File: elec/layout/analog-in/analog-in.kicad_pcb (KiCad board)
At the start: 2 copper layers, 8 parts, among them U2 1µF ±10% 25V X5R, U3 10kΩ ±1% 62.5mW, U4 10kΩ ±1% 62.5mW, U6 1kΩ ±1% 62.5mW, U7 1kΩ ±1% 62.5mW

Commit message: rebuild all modules
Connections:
- net io renamed top

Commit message: core layout, rebuild modules with compiler updates
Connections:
- U1 pad 10: line-1 -> line
- U1 pad 9: line -> line-1
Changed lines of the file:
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@@
     (net 4 "AIN2")
     (net 5 "AIN1")
-    (net 6 "line")
+    (net 6 "line-1")
     (net 7 "gnd")
-    (net 8 "line-1")
+    (net 8 "line")
     (net 9 "ALERT_slash_RDY")
     (net 10 "amplifier.opamp.footprint.pins[4].net-net")
@@
             (layers "F.Cu" "F.Paste" "F.Mask")
             (remove_unused_layers no)
-            (net 6 "line"))
+            (net 6 "line-1"))
         (pad "10" smd oval
             (at -1 -2.11 90)
@@
             (layers "F.Cu" "F.Paste" "F.Mask")
             (remove_unused_layers no)
-            (net 8 "line-1"))
+            (net 8 "line"))
         (model "/Users/narayanpowderly/projects/hil-blocks/build/footprints/footprints.3dshapes/MSOP-10_L3.0-W3.0-H1.1-LS5.0-P0.50.step"
             (offset

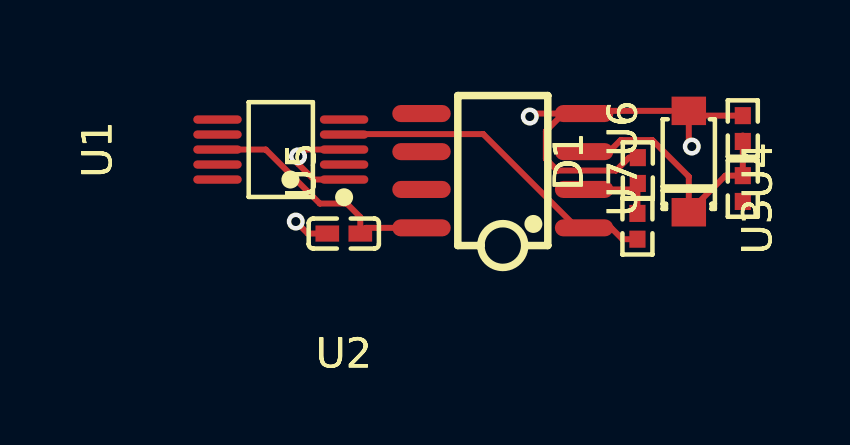
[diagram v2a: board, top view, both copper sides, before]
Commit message: update analog in
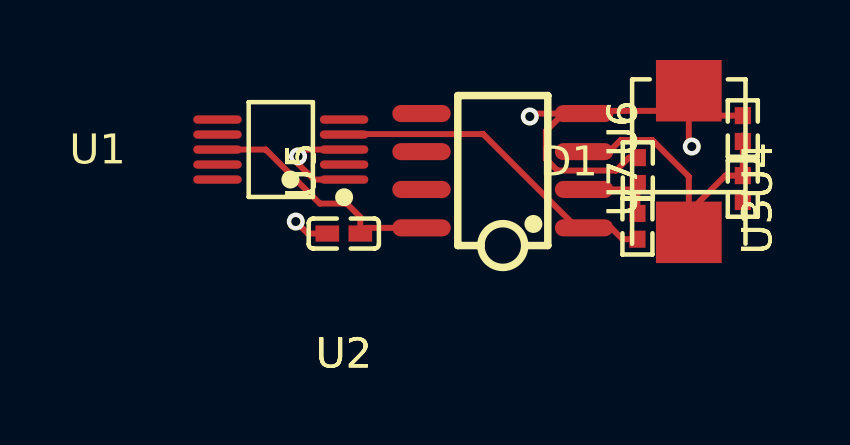
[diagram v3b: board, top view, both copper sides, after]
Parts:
- D1: footprint atopile:SOD-123_L2.8-W1.8-LS3.7-RD-5bef17 -> atopile:SMB_L4.6-W3.6-LS5.3-RD-330cb3
- U1: footprint lib:MSOP-10_L3.0-W3.0-P0.50-LS5.0-BL -> atopile:MSOP-10_L3.0-W3.0-P0.50-LS5.0-BL-752175
- U3, U4: value 10kΩ ±1% 62.5mW -> 1kΩ ±1% 62.5mW
- U5: value (none) -> BW CMRR Ib Vos GBW Iout SR
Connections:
- net AIN1 renamed adc-line-4
- net AIN2 renamed adc-line-2
- net AIN3 renamed adc-line-1
- net ALERT_slash_RDY renamed adc-line-3
- net cathode renamed line-2
- net inverting renamed inverting_input
- U1 pad 10: line -> line-1
- U1 pad 9: line-1 -> line

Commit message: Everything builds
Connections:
- D1 pad 1: line-2 -> line-1
- D1 pad 2: gnd -> adc-line-4
- U1 pad 1: gnd -> adc-line-4
- U1 pad 10: line-1 -> line
- U1 pad 2: adc-line-3 -> adc-line-2
- U1 pad 3: gnd -> adc-line-4
- U1 pad 5: adc-line-4 -> adc-line-3
- U1 pad 6: adc-line-2 -> adc-line-1
- U1 pad 7: adc-line-1 -> adc-line
- U1 pad 9: line -> line-3
- U2 pad 2: gnd -> adc-line-4
- U4 pad 1: gnd -> adc-line-4
- U5 pad 3: line-2 -> line-1
- U5 pad 4: gnd -> adc-line-4
- U6 pad 1: line-2 -> line-1
- U6 pad 2: gnd -> adc-line-4
- U7 pad 1: top -> line-2
- U7 pad 2: line-2 -> line-1
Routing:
- net gnd: track 18.6 -> 0.00 mm, vias 4 -> 0
- net adc-line-4: track 0.00 -> 18.6 mm, vias 0 -> 4
- net line-2: track 8.99 -> 0.00 mm
- net line-1: track 0.00 -> 8.99 mm
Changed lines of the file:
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@@
     (net 0 "")
     (net 1 "amplifier.opamp.footprint.pins[5].net-net")
-    (net 2 "line-2")
+    (net 2 "line-1")
     (net 3 "amplifier.opamp.footprint.pins[6].net-net")
-    (net 4 "adc-line-2")
-    (net 5 "adc-line-4")
-    (net 6 "line")
-    (net 7 "gnd")
-    (net 8 "line-1")
-    (net 9 "adc-line-3")
+    (net 4 "adc-line-1")
+    (net 5 "adc-line-3")
+    (net 6 "line-3")
+    (net 7 "adc-line-4")
+    (net 8 "line")
+    (net 9 "adc-line-2")
     (net 10 "amplifier.opamp.footprint.pins[4].net-net")
-    (net 11 "top")
+    (net 11 "line-2")
     (net 12 "inverting_input")
-    (net 13 "adc-line-1")
+    (net 13 "adc-line")
     (net 14 "output")
     (net 15 "hv")
@@
             (layers "F.Cu" "F.Paste" "F.Mask")
             (remove_unused_layers no)
-            (net 7 "gnd"))
+            (net 7 "adc-line-4"))
         (pad "1" smd rect
             (at -2.36 0 90)
@@
             (layers "F.Cu" "F.Paste" "F.Mask")
             (remove_unused_layers no)
-            (net 2 "line-2")))
+            (net 2 "line-1")))
     (footprint "atopile:SOIC-8_L5.0-W4.0-P1.27-LS6.0-BL-294f77"
         (layer "F.Cu")
@@
             (layers "F.Cu" "F.Paste" "F.Mask")
             (remove_unused_layers no)
-            (net 2 "line-2"))
+            (net 2 "line-1"))
         (pad "4" smd oval
             (at 1.9 2.71 90)
@@
             (layers "F.Cu" "F.Paste" "F.Mask")
             (remove_unused_layers no)
-            (net 7 "gnd"))
+            (net 7 "adc-line-4"))
         (pad "5" smd oval
             (at 1.9 -2.71 90)
@@
             (layers "F.Cu" "F.Paste" "F.Mask")
             (remove_unused_layers no)
-            (net 7 "gnd"))
+            (net 7 "adc-line-4"))
         (pad "2" smd rect
             (at 0.43 0 270)
@@
             (layers "F.Cu" "F.Paste" "F.Mask")
             (remove_unused_layers no)
-            (net 11 "top"))
+            (net 11 "line-2"))
         (pad "2" smd rect
             (at 0.43 0 90)
@@
             (layers "F.Cu" "F.Paste" "F.Mask")
             (remove_unused_layers no)
-            (net 2 "line-2")))
+            (net 2 "line-1")))
     (footprint "atopile:R0402-56259e"
         (layer "F.Cu")
@@
             (layers "F.Cu" "F.Paste" "F.Mask")
             (remove_unused_layers no)
-            (net 2 "line-2"))
+            (net 2 "line-1"))
         (pad "2" smd rect
             (at 0.43 0 90)
@@
             (layers "F.Cu" "F.Paste" "F.Mask")
             (remove_unused_layers no)
-            (net 7 "gnd")))
+            (net 7 "adc-line-4")))
     (footprint "atopile:MSOP-10_L3.0-W3.0-P0.50-LS5.0-BL-752175"
         (layer "F.Cu")
@@
             (layers "F.Cu" "F.Paste" "F.Mask")
             (remove_unused_layers no)
-            (net 7 "gnd"))
+            (net 7 "adc-line-4"))
         (pad "2" smd oval
             (at -0.5 2.11 90)
@@
             (layers "F.Cu" "F.Paste" "F.Mask")
             (remove_unused_layers no)
-            (net 9 "adc-line-3"))
+            (net 9 "adc-line-2"))
         (pad "3" smd oval
             (at 0 2.11 90)
@@
             (layers "F.Cu" "F.Paste" "F.Mask")
             (remove_unused_layers no)
-            (net 7 "gnd"))
+            (net 7 "adc-line-4"))
         (pad "4" smd oval
             (at 0.5 2.11 90)
@@
             (layers "F.Cu" "F.Paste" "F.Mask")
             (remove_unused_layers no)
-            (net 5 "adc-line-4"))
+            (net 5 "adc-line-3"))
         (pad "10" smd oval
             (at -1 -2.11 90)
@@
             (layers "F.Cu" "F.Paste" "F.Mask")
             (remove_unused_layers no)
-            (net 8 "line-1"))
+            (net 8 "line"))
         (pad "9" smd oval
             (at -0.5 -2.11 90)
@@
             (layers "F.Cu" "F.Paste" "F.Mask")
             (remove_unused_layers no)
-            (net 6 "line"))
+            (net 6 "line-3"))
         (pad "8" smd oval
             (at 0 -2.11 90)
@@
             (layers "F.Cu" "F.Paste" "F.Mask")
             (remove_unused_layers no)
-            (net 13 "adc-line-1"))
+            (net 13 "adc-line"))
         (pad "6" smd oval
             (at 1 -2.11 90)
@@
             (layers "F.Cu" "F.Paste" "F.Mask")
             (remove_unused_layers no)
-            (net 4 "adc-line-2")))
+            (net 4 "adc-line-1")))
     (footprint "atopile:C0402-b3ef17"
         (layer "F.Cu")
@@
             (layers "F.Cu" "F.Paste" "F.Mask")
             (remove_unused_layers no)
-            (net 7 "gnd")))
+            (net 7 "adc-line-4")))
     (via
         (at 131.8 106.9)

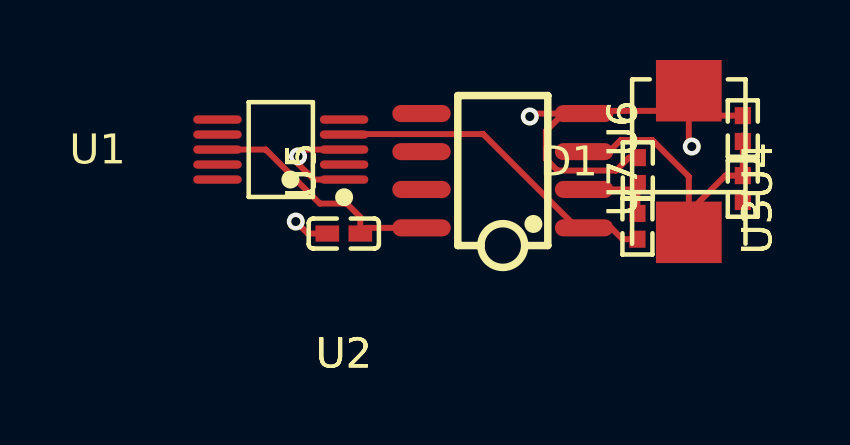
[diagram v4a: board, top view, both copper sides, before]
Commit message: update syntax, delete vendored packages
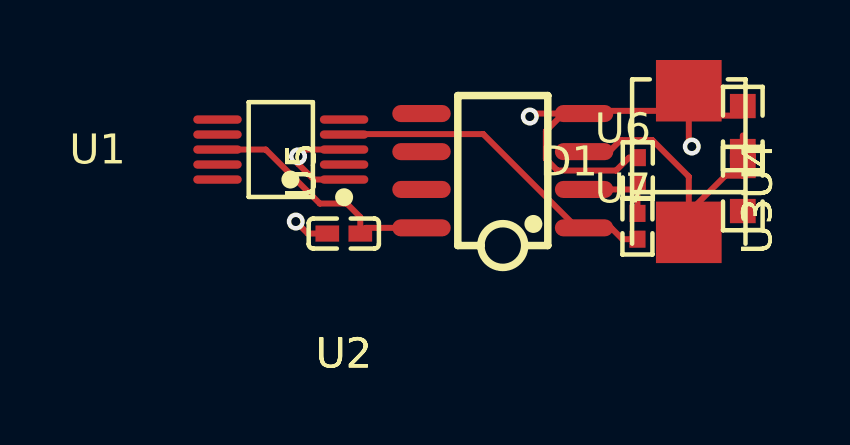
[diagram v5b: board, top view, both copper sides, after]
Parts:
- U3, U4: value 1kΩ ±1% 62.5mW -> 10kΩ ±1% 62.5mW
- U6, U7: value 1kΩ ±1% 62.5mW -> 10kΩ ±1% 100mW; footprint atopile:R0402-56259e -> atopile:R0603-ebcab9
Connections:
- U1 pad 10: line -> line-2
- U1 pad 2: adc-line-2 -> adc-line
- U1 pad 5: adc-line-3 -> adc-line-2
- U1 pad 7: adc-line -> adc-line-3
- U7 pad 1: line-2 -> line

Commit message: build and re-link layouts
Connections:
- D1 pad 1: line-1 -> line-2
- D1 pad 2: adc-line-4 -> adc-line
- U1 pad 1: adc-line-4 -> adc-line
- U1 pad 10: line-2 -> line
- U1 pad 2: adc-line -> adc-line-1
- U1 pad 3: adc-line-4 -> adc-line
- U1 pad 5: adc-line-2 -> adc-line-3
- U1 pad 6: adc-line-1 -> adc-line-2
- U1 pad 7: adc-line-3 -> adc-line-4
- U1 pad 9: line-3 -> line-1
- U2 pad 2: adc-line-4 -> adc-line
- U4 pad 1: adc-line-4 -> adc-line
- U5 pad 3: line-1 -> line-2
- U5 pad 4: adc-line-4 -> adc-line
- U6 pad 1: line-1 -> line-2
- U6 pad 2: adc-line-4 -> adc-line
- U7 pad 1: line -> line-3
- U7 pad 2: line-1 -> line-2
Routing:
- net adc-line-4: track 18.6 -> 0.00 mm, vias 4 -> 0
- net adc-line: track 0.00 -> 18.6 mm, vias 0 -> 4
- net line-2: track 0.00 -> 8.99 mm
- net line-1: track 8.99 -> 0.00 mm
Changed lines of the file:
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@@
     (net 0 "")
     (net 1 "amplifier.opamp.footprint.pins[5].net-net")
-    (net 2 "line-1")
+    (net 2 "line-2")
     (net 3 "amplifier.opamp.footprint.pins[6].net-net")
-    (net 4 "adc-line-1")
-    (net 5 "adc-line-2")
-    (net 6 "line-3")
-    (net 7 "adc-line-4")
-    (net 8 "line-2")
-    (net 9 "adc-line")
+    (net 4 "adc-line-2")
+    (net 5 "adc-line-3")
+    (net 6 "line-1")
+    (net 7 "adc-line")
+    (net 8 "line")
+    (net 9 "adc-line-1")
     (net 10 "amplifier.opamp.footprint.pins[4].net-net")
-    (net 11 "line")
+    (net 11 "line-3")
     (net 12 "inverting_input")
-    (net 13 "adc-line-3")
+    (net 13 "adc-line-4")
     (net 14 "output")
     (net 15 "hv")
@@
             (layers "F.Cu" "F.Paste" "F.Mask")
             (remove_unused_layers no)
-            (net 7 "adc-line-4"))
+            (net 7 "adc-line"))
         (pad "1" smd rect
             (at -2.36 0 90)
@@
             (layers "F.Cu" "F.Paste" "F.Mask")
             (remove_unused_layers no)
-            (net 2 "line-1")))
+            (net 2 "line-2")))
     (footprint "atopile:SOIC-8_L5.0-W4.0-P1.27-LS6.0-BL-294f77"
         (layer "F.Cu")
@@
             (layers "F.Cu" "F.Paste" "F.Mask")
             (remove_unused_layers no)
-            (net 2 "line-1"))
+            (net 2 "line-2"))
         (pad "4" smd oval
             (at 1.9 2.71 90)
@@
             (layers "F.Cu" "F.Paste" "F.Mask")
             (remove_unused_layers no)
-            (net 7 "adc-line-4"))
+            (net 7 "adc-line"))
         (pad "5" smd oval
             (at 1.9 -2.71 90)
@@
             (layers "F.Cu" "F.Paste" "F.Mask")
             (remove_unused_layers no)
-            (net 7 "adc-line-4"))
+            (net 7 "adc-line"))
         (pad "2" smd rect
             (at 0.43 0 270)
@@
             (layers "F.Cu" "F.Paste" "F.Mask")
             (remove_unused_layers no)
-            (net 2 "line-1"))
+            (net 2 "line-2"))
         (pad "1" smd rect
             (at -0.75 0 90)
@@
             (layers "F.Cu" "F.Paste" "F.Mask")
             (remove_unused_layers no)
-            (net 11 "line")))
+            (net 11 "line-3")))
     (footprint "atopile:R0603-ebcab9"
         (layer "F.Cu")
@@
             (layers "F.Cu" "F.Paste" "F.Mask")
             (remove_unused_layers no)
-            (net 7 "adc-line-4"))
+            (net 7 "adc-line"))
         (pad "1" smd rect
             (at -0.75 0 90)
@@
             (layers "F.Cu" "F.Paste" "F.Mask")
             (remove_unused_layers no)
-            (net 2 "line-1")))
+            (net 2 "line-2")))
     (footprint "atopile:MSOP-10_L3.0-W3.0-P0.50-LS5.0-BL-752175"
         (layer "F.Cu")
@@
             (layers "F.Cu" "F.Paste" "F.Mask")
             (remove_unused_layers no)
-            (net 7 "adc-line-4"))
+            (net 7 "adc-line"))
         (pad "2" smd oval
             (at -0.5 2.11 90)
@@
             (layers "F.Cu" "F.Paste" "F.Mask")
             (remove_unused_layers no)
-            (net 9 "adc-line"))
+            (net 9 "adc-line-1"))
         (pad "3" smd oval
             (at 0 2.11 90)
@@
             (layers "F.Cu" "F.Paste" "F.Mask")
             (remove_unused_layers no)
-            (net 7 "adc-line-4"))
+            (net 7 "adc-line"))
         (pad "4" smd oval
             (at 0.5 2.11 90)
@@
             (layers "F.Cu" "F.Paste" "F.Mask")
             (remove_unused_layers no)
-            (net 5 "adc-line-2"))
+            (net 5 "adc-line-3"))
         (pad "10" smd oval
             (at -1 -2.11 90)
@@
             (layers "F.Cu" "F.Paste" "F.Mask")
             (remove_unused_layers no)
-            (net 8 "line-2"))
+            (net 8 "line"))
         (pad "9" smd oval
             (at -0.5 -2.11 90)
@@
             (layers "F.Cu" "F.Paste" "F.Mask")
             (remove_unused_layers no)
-            (net 6 "line-3"))
+            (net 6 "line-1"))
         (pad "8" smd oval
             (at 0 -2.11 90)
@@
             (layers "F.Cu" "F.Paste" "F.Mask")
             (remove_unused_layers no)
-            (net 13 "adc-line-3"))
+            (net 13 "adc-line-4"))
         (pad "6" smd oval
             (at 1 -2.11 90)
@@
             (layers "F.Cu" "F.Paste" "F.Mask")
             (remove_unused_layers no)
-            (net 4 "adc-line-1")))
+            (net 4 "adc-line-2")))
     (footprint "atopile:C0402-b3ef17"
         (layer "F.Cu")
@@
             (layers "F.Cu" "F.Paste" "F.Mask")
             (remove_unused_layers no)
-            (net 7 "adc-line-4")))
+            (net 7 "adc-line")))
     (via
         (at 131.8 106.9)

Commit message: all modules building
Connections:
- D1 pad 1: line-2 -> line-1
- D1 pad 2: adc-line -> gnd
- U1 pad 1: adc-line -> gnd
- U1 pad 10: line -> line-2
- U1 pad 3: adc-line -> gnd
- U1 pad 5: adc-line-3 -> adc-line-4
- U1 pad 6: adc-line-2 -> adc-line-3
- U1 pad 7: adc-line-4 -> adc-line
- U1 pad 9: line-1 -> line
- U2 pad 2: adc-line -> gnd
- U4 pad 1: adc-line -> gnd
- U5 pad 3: line-2 -> line-1
- U5 pad 4: adc-line -> gnd
- U6 pad 1: line-2 -> line-1
- U6 pad 2: adc-line -> gnd
- U7 pad 2: line-2 -> line-1
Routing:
- net gnd: track 0.00 -> 18.6 mm, vias 0 -> 4
- net adc-line: track 18.6 -> 0.00 mm, vias 4 -> 0
- net line-2: track 8.99 -> 0.00 mm
- net line-1: track 0.00 -> 8.99 mm
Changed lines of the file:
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@@
     (net 0 "")
     (net 1 "amplifier.opamp.footprint.pins[5].net-net")
-    (net 2 "line-2")
+    (net 2 "line-1")
     (net 3 "amplifier.opamp.footprint.pins[6].net-net")
-    (net 4 "adc-line-2")
-    (net 5 "adc-line-3")
-    (net 6 "line-1")
-    (net 7 "adc-line")
-    (net 8 "line")
+    (net 4 "adc-line-3")
+    (net 5 "adc-line-4")
+    (net 6 "line")
+    (net 7 "gnd")
+    (net 8 "line-2")
     (net 9 "adc-line-1")
     (net 10 "amplifier.opamp.footprint.pins[4].net-net")
     (net 11 "line-3")
     (net 12 "inverting_input")
-    (net 13 "adc-line-4")
+    (net 13 "adc-line")
     (net 14 "output")
     (net 15 "hv")
@@
             (layers "F.Cu" "F.Paste" "F.Mask")
             (remove_unused_layers no)
-            (net 7 "adc-line"))
+            (net 7 "gnd"))
         (pad "1" smd rect
             (at -2.36 0 90)
@@
             (layers "F.Cu" "F.Paste" "F.Mask")
             (remove_unused_layers no)
-            (net 2 "line-2")))
+            (net 2 "line-1")))
     (footprint "atopile:SOIC-8_L5.0-W4.0-P1.27-LS6.0-BL-294f77"
         (layer "F.Cu")
@@
             (layers "F.Cu" "F.Paste" "F.Mask")
             (remove_unused_layers no)
-            (net 2 "line-2"))
+            (net 2 "line-1"))
         (pad "4" smd oval
             (at 1.9 2.71 90)
@@
             (layers "F.Cu" "F.Paste" "F.Mask")
             (remove_unused_layers no)
-            (net 7 "adc-line"))
+            (net 7 "gnd"))
         (pad "5" smd oval
             (at 1.9 -2.71 90)
@@
             (layers "F.Cu" "F.Paste" "F.Mask")
             (remove_unused_layers no)
-            (net 7 "adc-line"))
+            (net 7 "gnd"))
         (pad "2" smd rect
             (at 0.43 0 270)
@@
             (layers "F.Cu" "F.Paste" "F.Mask")
             (remove_unused_layers no)
-            (net 2 "line-2"))
+            (net 2 "line-1"))
         (pad "1" smd rect
             (at -0.75 0 90)
@@
             (layers "F.Cu" "F.Paste" "F.Mask")
             (remove_unused_layers no)
-            (net 7 "adc-line"))
+            (net 7 "gnd"))
         (pad "1" smd rect
             (at -0.75 0 90)
@@
             (layers "F.Cu" "F.Paste" "F.Mask")
             (remove_unused_layers no)
-            (net 2 "line-2")))
+            (net 2 "line-1")))
     (footprint "atopile:MSOP-10_L3.0-W3.0-P0.50-LS5.0-BL-752175"
         (layer "F.Cu")
@@
             (layers "F.Cu" "F.Paste" "F.Mask")
             (remove_unused_layers no)
-            (net 7 "adc-line"))
+            (net 7 "gnd"))
         (pad "2" smd oval
             (at -0.5 2.11 90)
@@
             (layers "F.Cu" "F.Paste" "F.Mask")
             (remove_unused_layers no)
-            (net 7 "adc-line"))
+            (net 7 "gnd"))
         (pad "4" smd oval
             (at 0.5 2.11 90)
@@
             (layers "F.Cu" "F.Paste" "F.Mask")
             (remove_unused_layers no)
-            (net 5 "adc-line-3"))
+            (net 5 "adc-line-4"))
         (pad "10" smd oval
             (at -1 -2.11 90)
@@
             (layers "F.Cu" "F.Paste" "F.Mask")
             (remove_unused_layers no)
-            (net 8 "line"))
+            (net 8 "line-2"))
         (pad "9" smd oval
             (at -0.5 -2.11 90)
@@
             (layers "F.Cu" "F.Paste" "F.Mask")
             (remove_unused_layers no)
-            (net 6 "line-1"))
+            (net 6 "line"))
         (pad "8" smd oval
             (at 0 -2.11 90)
@@
             (layers "F.Cu" "F.Paste" "F.Mask")
             (remove_unused_layers no)
-            (net 13 "adc-line-4"))
+            (net 13 "adc-line"))
         (pad "6" smd oval
             (at 1 -2.11 90)
@@
             (layers "F.Cu" "F.Paste" "F.Mask")
             (remove_unused_layers no)
-            (net 4 "adc-line-2")))
+            (net 4 "adc-line-3")))
     (footprint "atopile:C0402-b3ef17"
         (layer "F.Cu")
@@
             (layers "F.Cu" "F.Paste" "F.Mask")
             (remove_unused_layers no)
-            (net 7 "adc-line")))
+            (net 7 "gnd")))
     (via
         (at 131.8 106.9)
